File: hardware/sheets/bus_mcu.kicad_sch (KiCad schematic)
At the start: 52 parts, among them M1 Core2350B (0MB PSRAM), U10 74HC161, U11 74HC161, U12 74HCT165, U13 74LVC245A, U14 74HCT244, U15 74HCT244, U16 74HCT244, U17 74HCT04, U18 74HC08, U2 74LVC245A, U3 74LVC245A, U4 74LVC245A, U5 74LVC245A, U6 74LVC245A, U7 74HC161, U8 74HC161, U9 74HC161

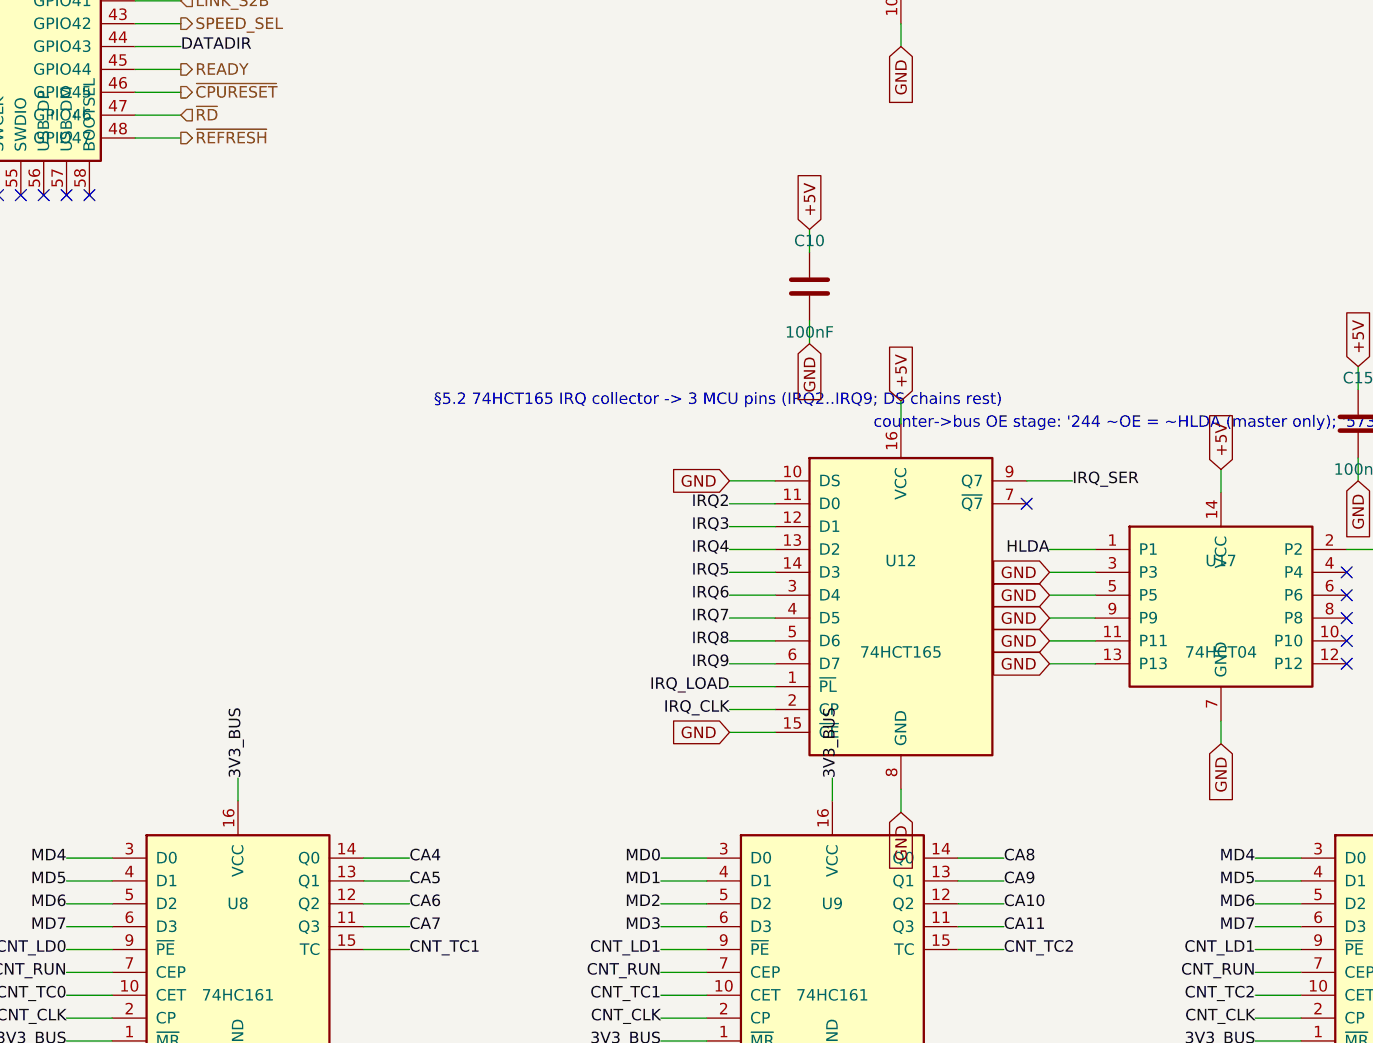
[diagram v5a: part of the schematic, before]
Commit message: Storage: on-board only, IRQ14-default strap; 16-bit IRQ collector
Remove card_storage (same rationale as COM/LPT/RTC -- the on-board sheet
carries the full jumper set; ~25-line wrapper, restorable from git).
Standalone PCBs remaining: video + the isatest jig.

- storage: JP3 IRQ strap -- 1-2 = IRQ14 (DEFAULT, the AT primary-IDE
  convention), 2-3 = IRQ5 (XT fallback; also the LPT alternate), open =
  polled. The '125 now drives STOR_IRQ into the strap, so the unselected
  line is untouched.
- bus_mcu: IRQ14 had no physical path into the soft-PIC, so the IRQ
  collector is now a cascaded pair of 74HCT165s (U19 IRQ10-15 -> U12
  IRQ2-9, net IRQ_CAS), with R19-R24 idle pull-downs and C18. Zero GPIO
  cost -- same IRQ_LOAD/IRQ_CLK/IRQ_SER, firmware shifts 16 bits. Also
  un-dangles the IRQ10-15 interface pins the sheet had declared since day
  one. IRQ10-15 are motherboard-internal (the 60-pin header carries only
  IRQ2-8).
- README: XT-IDE moves into the on-board peripherals list (all three
  straps + the shadow-loaded-BIOS note); motherboard is the third board;
  coexistence example now pairs the on-board XT-IDE with a real ISA IDE
  card at 0x320.
- Design doc: 4.3 card list, 10 JP3 strap + XTIDE UB IRQ-config note
  (was still "Poll or IRQ5"), 5.2 collector row, 14 IRQ table (IRQ14 no
  longer "spare"), 15 BOM row. Decisions logged in open-questions.md,
  questions-storage.md, questions-bus_mcu.md.

Verified: motherboard + both cards rebuild with zero structural ERC;
netlist shows /IRQ14 = {JP3, pull-down, U19 collector input} spanning
storage<->bus_mcu, IRQ_CAS = U19.Q7 -> U12.DS, and /IRQ5 still carrying
sidecar + LPT strap + collector.

Co-Authored-By: Claude Fable 5 <noreply@anthropic.com>
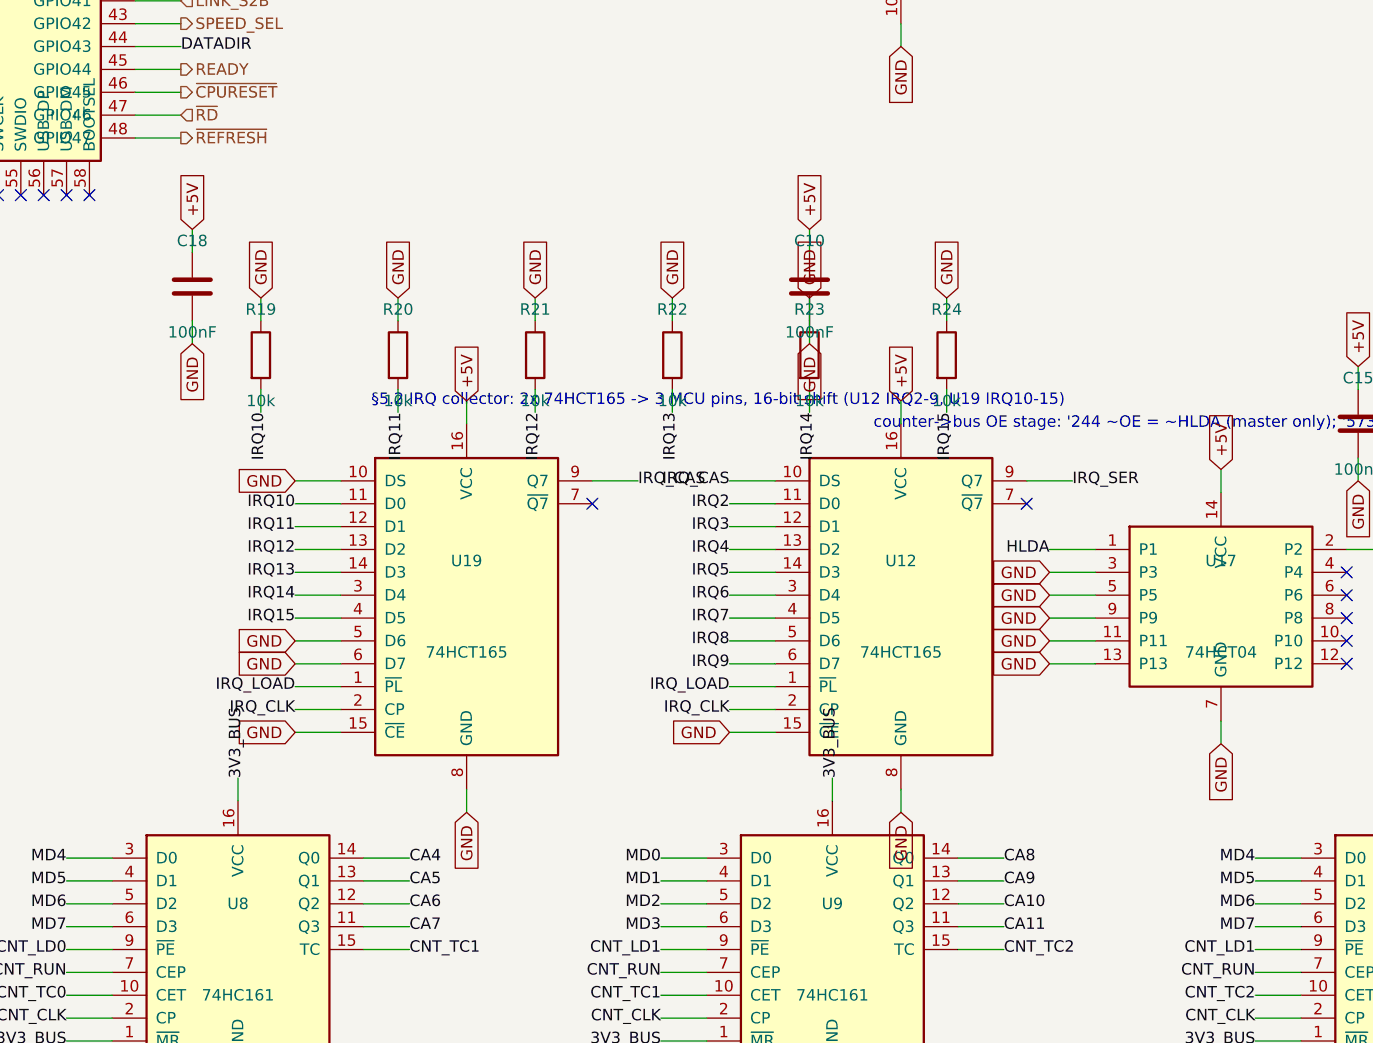
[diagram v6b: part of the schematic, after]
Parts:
- added C18: 100nF, symbol Device:C
- added R19, R20, R21, R22, R23, R24: 10k, symbol Device:R
- added U19: 74HCT165, symbol mini-xt:74HCT165
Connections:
- net +5V: now also C18.1, U19.16 (VCC)
- net GND: now also C18.2, R19.1, R20.1, R21.1, R22.1, R23.1, R24.1, U19.10 (DS), U19.15 (~{CE}), U19.5 (D6), U19.6 (D7), U19.8 (GND); no longer U12.10 (DS)
- net IRQ10: now also R19.2, U19.11 (D0)
- net IRQ11: now also R20.2, U19.12 (D1)
- net IRQ12: now also R21.2, U19.13 (D2)
- net IRQ13: now also R22.2, U19.14 (D3)
- net IRQ14: now also R23.2, U19.3 (D4)
- net IRQ15: now also R24.2, U19.4 (D5)
- net IRQ_CLK: now also U19.2 (CP)
- net IRQ_LOAD: now also U19.1 (~{PL})
- new net IRQ_CAS: U12.10 (DS), U19.9 (Q7)
- no-connect marks 47 -> 48
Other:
- note added: "§5.2 IRQ collector: 2x 74HCT165 -> 3 MCU pins, 16-bit shift (U12 IRQ2-9, U19 IRQ10-15)"
- note removed: "§5.2 74HCT165 IRQ collector -> 3 MCU pins (IRQ2..IRQ9; DS chains rest)"

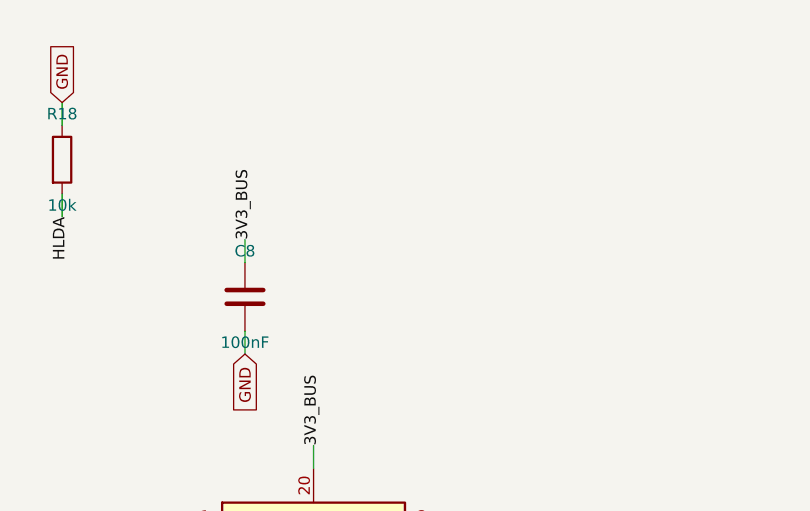
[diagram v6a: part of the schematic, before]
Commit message: Design-review fixes: reset parking, IRQ8 off the header, analog cleanups
Netlist-wide review sweep. IRQ8 leaves the 60-pin ISA header (pin 15 is a
second GND return; the on-board RTC owns IRQ8 exclusively, so its push-pull
drive is now correct by construction). Bus MCU Hi-Z parking completed:
~CPURESET pulled low (V20 held in reset while the MCU is unprogrammed),
~DACK1/~REFRESH parked deasserted, DRQ1 idled low. Supervisor 12 MHz crystal
damping R actually in series now (was parallel-to-nothing), plus a second
USBLC6 so both prog-port SW2 positions are ESD-protected. Audio: 0.5x PG
summing (MCP6002 headroom), 100k LINE bleed, unit B parked as a follower --
and the SUM stub moved off pin 5's row, where wiring unit B would have
silently merged SUM into VREF. CH224K VDD fed through 1k per the WCH ref
design. VGA blue ladder rescaled 1k/510 -> 820/470 (was ~12% blue-deficient).
Spare CMOS gate inputs grounded uniformly (cpu_core/rtc/storage); UART_RXD
pulled up (SIN idles at mark with JP1 open); dead pins/parts dropped
(com_port CLK, parallel RESET_DRV, storage R3). Bus CLK fixed at 7.16 MHz
logged as a decision. New passives mapped to JLC basic parts in parts.py.

Co-Authored-By: Claude Fable 5 <noreply@anthropic.com>
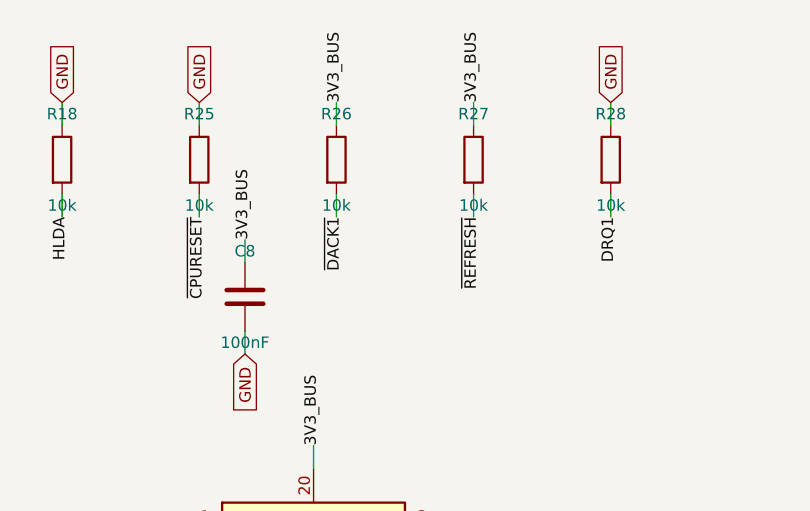
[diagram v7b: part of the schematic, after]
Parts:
- removed C1, C2, C6: 100nF, symbol Device:C
- removed C3: 10uF, symbol Device:C
- added C14, C15, C16, C17: 100nF, symbol Device:C
- added R25, R26, R27, R28: 10k, symbol Device:R
- C3: renamed from C9; value 100nF -> 10uF; LCSC Part Num C14663 -> C15850
- renumbered C7 to C1, C14 to C10, C16 to C12, C17 to C13, C15 to C18, C8 to C2, C10 to C6, C18 to C7, C12 to C8, C13 to C9
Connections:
- net +5V: now also C12.1, C13.1, C14.1, C15.1; no longer C6.1, C7.1, C8.1, C9.1
- net DRQ1: now also R28.2
- net GND: now also C6.1, C7.1, C8.1, C9.1, C14.2, C15.2, C16.1, C16.2, C17.1, C17.2, R25.1, R26.1, R27.1, R28.1; no longer C12.1, C13.1
- net ~{CPURESET}: now also R25.2
- net ~{DACK1}: now also R26.2
- net ~{REFRESH}: now also R27.2
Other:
- moved on the sheet: C1, C10, C12, C13, C18, C2, C3, C6, C7, C8, C9

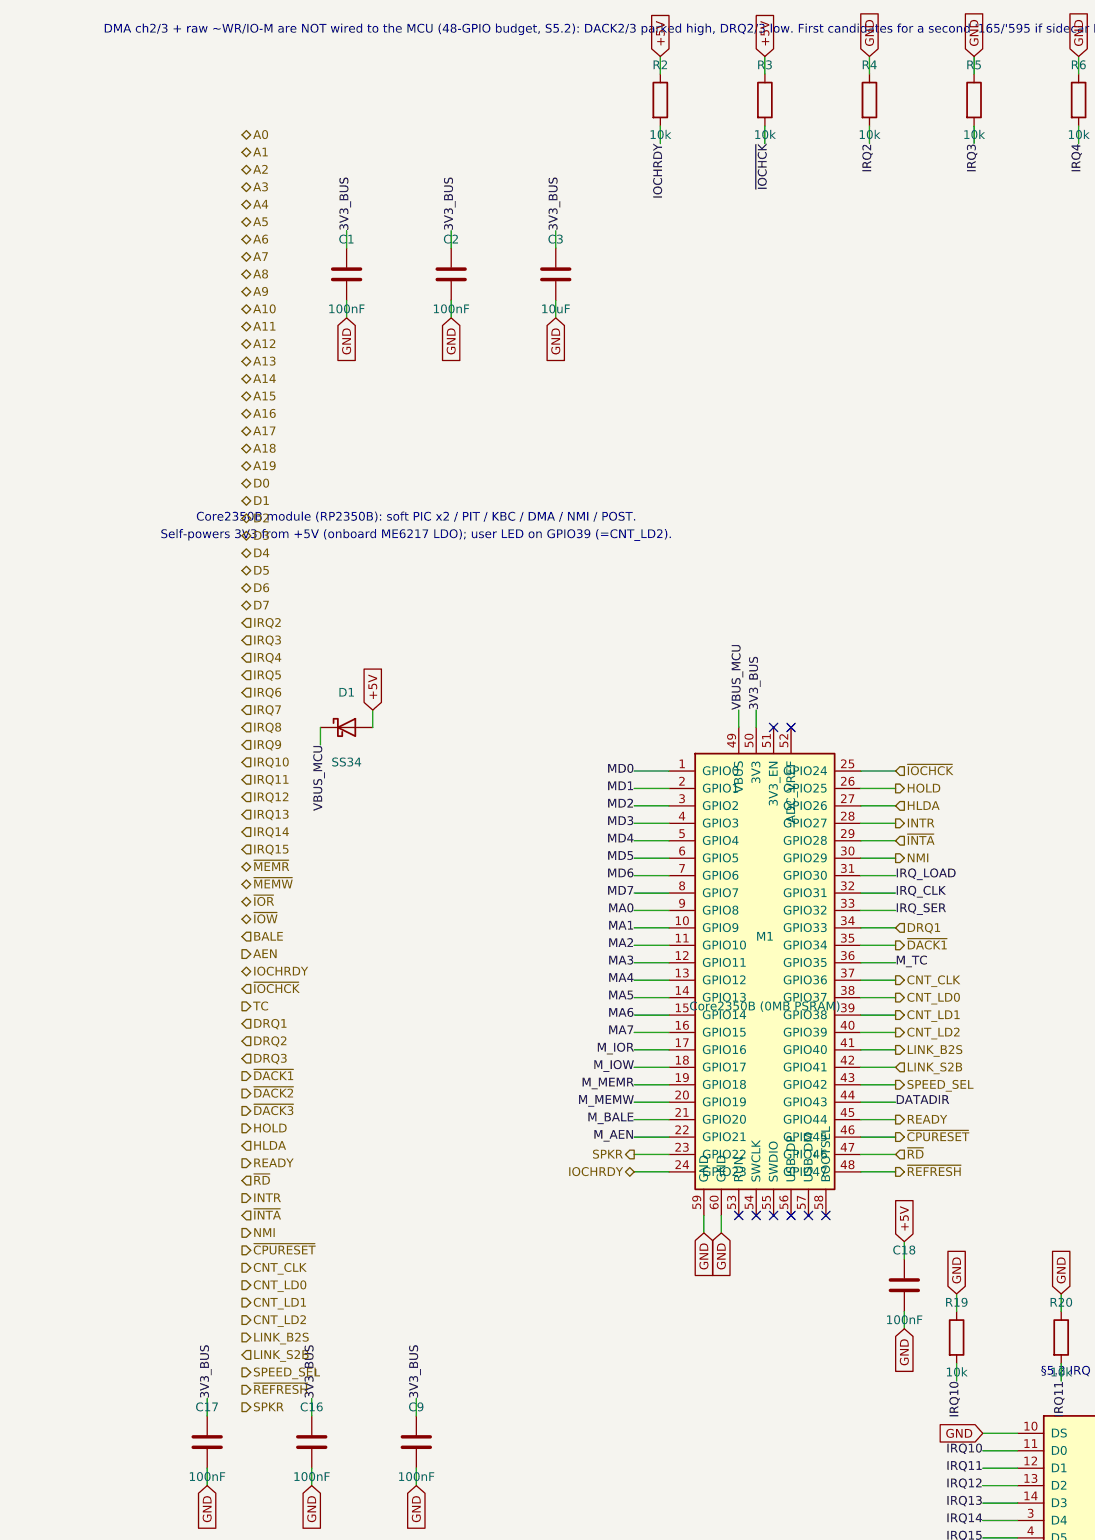
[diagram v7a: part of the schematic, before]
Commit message: ERC cleanup: NC flags on unused pins, anchored interface labels
KiCad 10 ERC drops from 366 to 16 violations, all noise:

- NC flags on the 36 genuinely unused pins (cpu_core '138/'161 spares,
  Supervisor RP2040 unused GPIO, Core2350B GPIO44-47, rtc '138 spares).
- emit_interface anchors every hier label on a stub wire ending in a
  same-name local label -- connectivity unchanged (still by name;
  netlist spans verified), but nothing dangles.
- Interface honesty: cpu_core drops AEN/IOCHRDY from PINS (both live on
  bus_mcu; nothing here touched them), bus_mcu drops PRIV_COUNTER (the
  counter chain is on-sheet, CNT_* never crosses).
- Remaining 6 label_dangling are root IRQ9-13/15: single-sheet by
  design (soft-PIC pull-ups await future 16-bit sources); kept in PINS
  as the AT-style contract.

Co-Authored-By: Claude Fable 5 <noreply@anthropic.com>
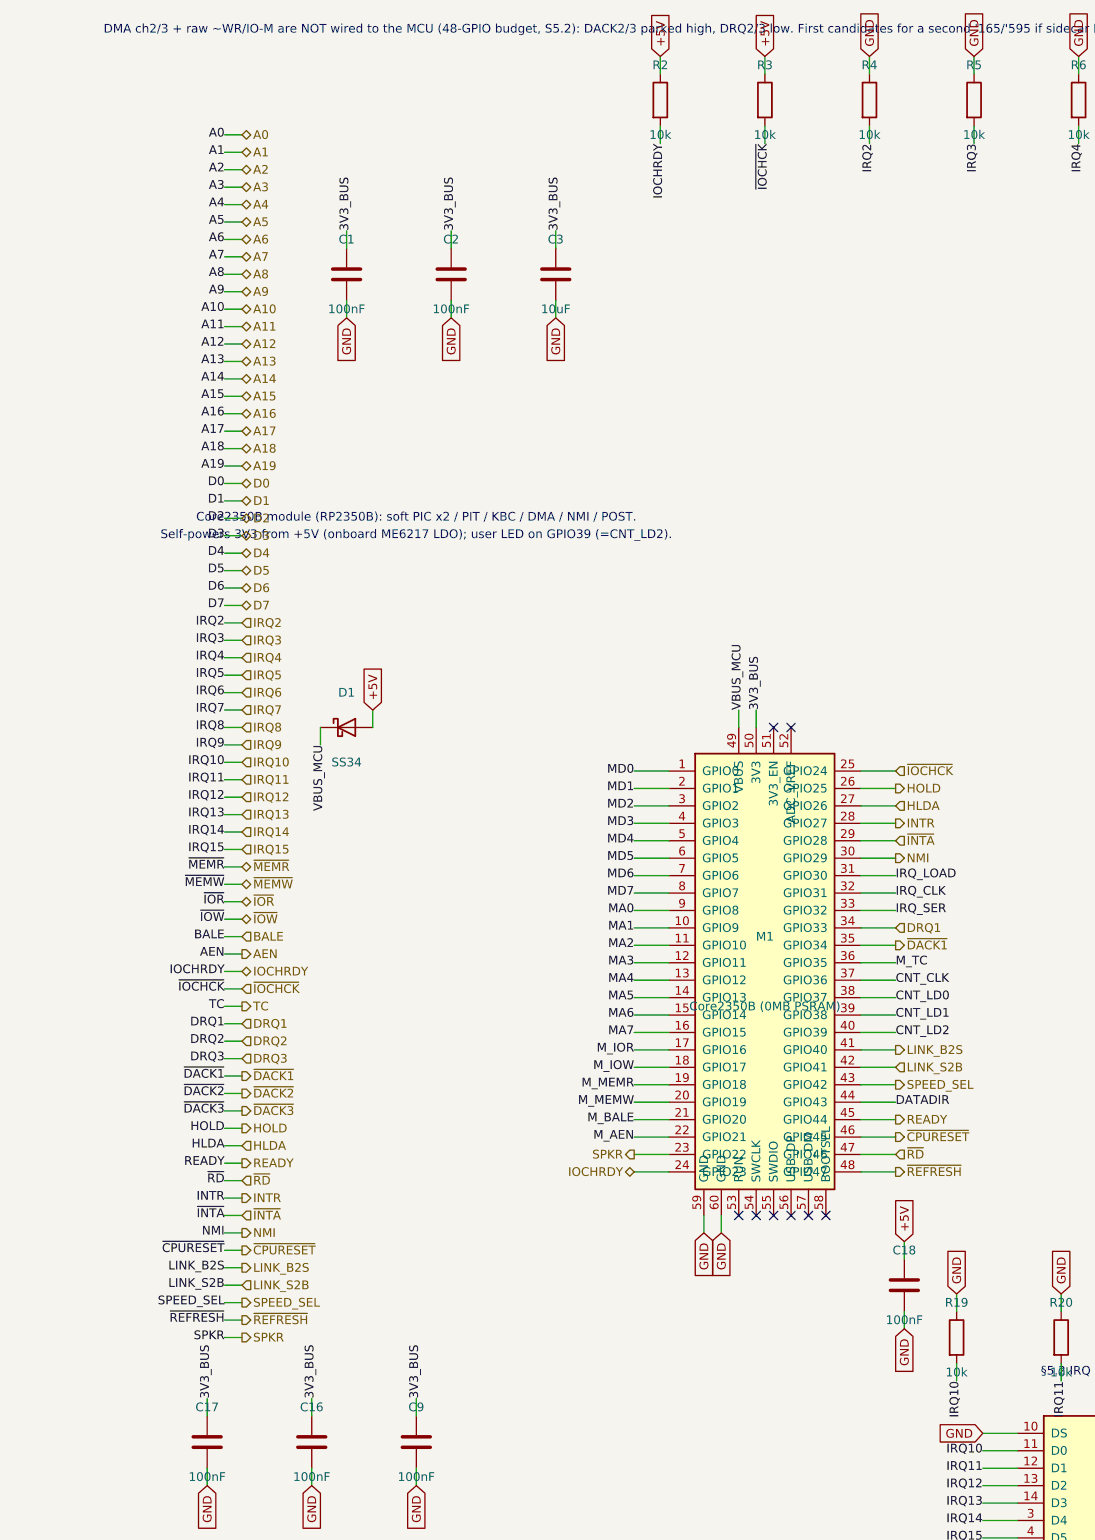
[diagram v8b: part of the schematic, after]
